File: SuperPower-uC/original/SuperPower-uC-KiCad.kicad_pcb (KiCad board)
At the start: 2 copper layers, 95 x 42 mm, 172 parts, among them J1 JST_PH_S2B_thru, J11 Conn_01x02_Male, J12 Conn_01x02_Male, J13 Conn_01x02_Male, J2 Barrel_Jack_Switch, J3 Conn_01x02_Male, J4 DNP/JST_ZH_S2B_thru, J5 JST_XH_S2B_thru, J6 Conn_01x02_Male, J7 Conn_01x19_Female, J8 Conn_01x19_Female, Q1 DMN2019UTS, Q10 2N7002A, Q11 2N7002A, Q12 DMP2035UVT, Q13 DMP2035UVT, Q14 DMP2035UVT, Q2 DMP3028LSD, Q3 DMN3018SSD, Q4 2N7002A, Q5 DMP2035UVT, Q6 BSS84-7-F, Q7 S8050, Q8 S8050, Q9 2N7002A, SW1 DNP/SKRKAEE020, U1 AP9101CK6-AYTRG1, U10 TPS63070RNMT, U2 USB-C, U3 IP4220CZ6, U4 LTC4162EUFD-LAD, U5 RV-3028-C7, U6 CP2102N-A01-GQFN28, U7 ESP32-WROOM32, U8 TPS70933DRVT, U9 TPS63070RNMT

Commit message: Update Placement + Add some labels
+3.3V Buck-Boost DC-DC converter
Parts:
- moved TP17 57.2 mm to (165.8, 64.5)
- moved TP5 26.2 mm to (120.8, 62.8)
- moved JP2 17.8 mm to (182.2, 60.2)
- moved R25 11.6 mm to (171.8, 64.2), turned to 0 degrees
- moved TP4 11.3 mm to (108.2, 56.0)
- moved TP7 8.88 mm to (102.0, 46.2)
- moved C24 8.67 mm to (172.8, 50.8), turned to 270 degrees
- moved TP6 8.30 mm to (102.0, 49.2)
- moved R54 7.24 mm to (179.5, 63.5), turned to 0 degrees
- moved R50 6.46 mm to (175.5, 50.0), turned to 180 degrees
- moved C19 6.15 mm to (172.8, 55.2), turned to 90 degrees
- moved Q10 5.54 mm to (175.8, 63.2), turned to 90 degrees
- moved R46 3.69 mm to (179.5, 53.2), turned to 0 degrees
- moved R42 3.62 mm to (179.0, 59.2), turned to 90 degrees
- moved C26 3.06 mm to (172.8, 46.8)
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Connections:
- net Net-(C16-Pad1) renamed /Regulator and Cut-Off Module/3v3_Vin
- net Net-(C22-Pad1) renamed /Regulator and Cut-Off Module/3v3_Vaux
- net Net-(JP2-Pad1) renamed /Regulator and Cut-Off Module/3v3_OnOff
- net Net-(L2-Pad1) renamed /Regulator and Cut-Off Module/3v3_L2
- net Net-(L2-Pad2) renamed /Regulator and Cut-Off Module/3v3_L1
- net Net-(Q5-Pad3) renamed /Regulator and Cut-Off Module/3v3_OnOff_Gate
- net Net-(R44-Pad1) renamed /Regulator and Cut-Off Module/3v3_EN
- net Net-(R46-Pad1) renamed /Regulator and Cut-Off Module/3v3_PG
- net Net-(R47-Pad2) renamed /Regulator and Cut-Off Module/3v3_FB

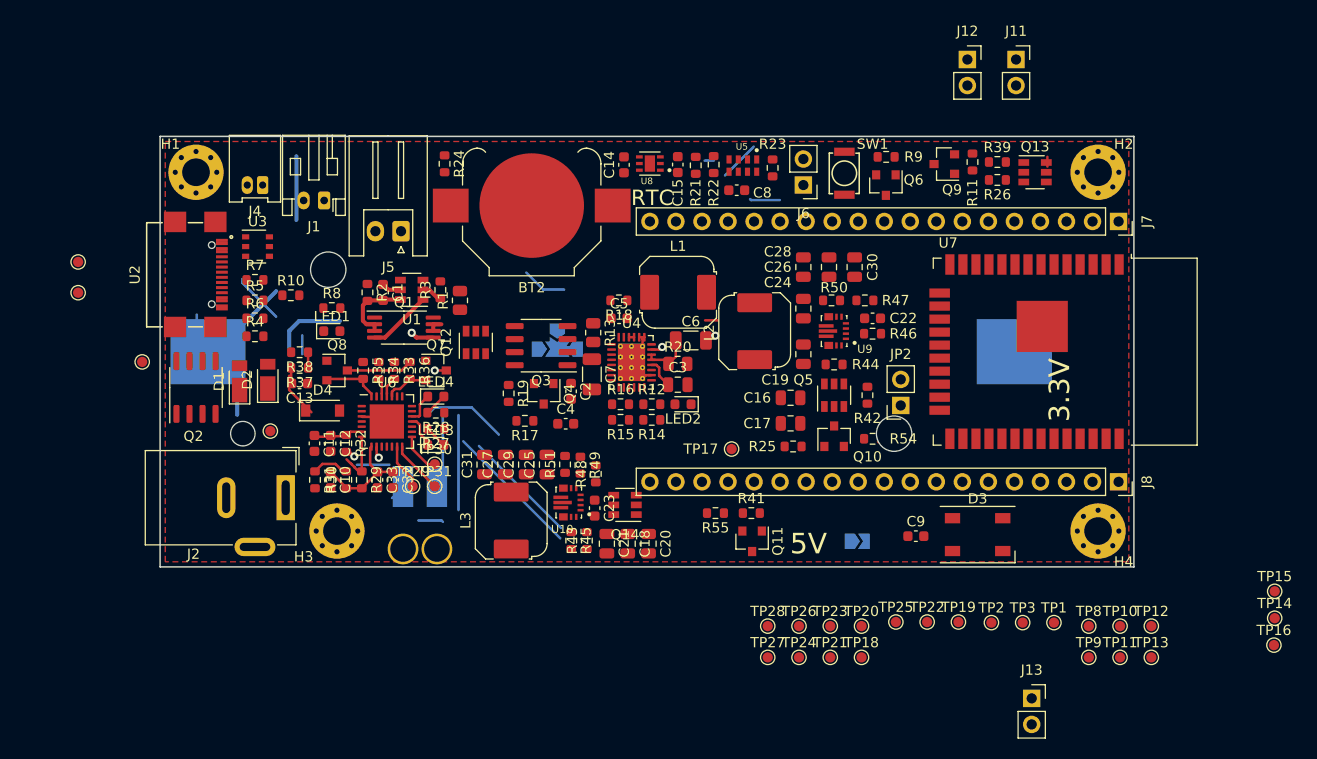
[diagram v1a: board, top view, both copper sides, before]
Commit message: Update Placement USB_UART_Bridge
+ Misc.
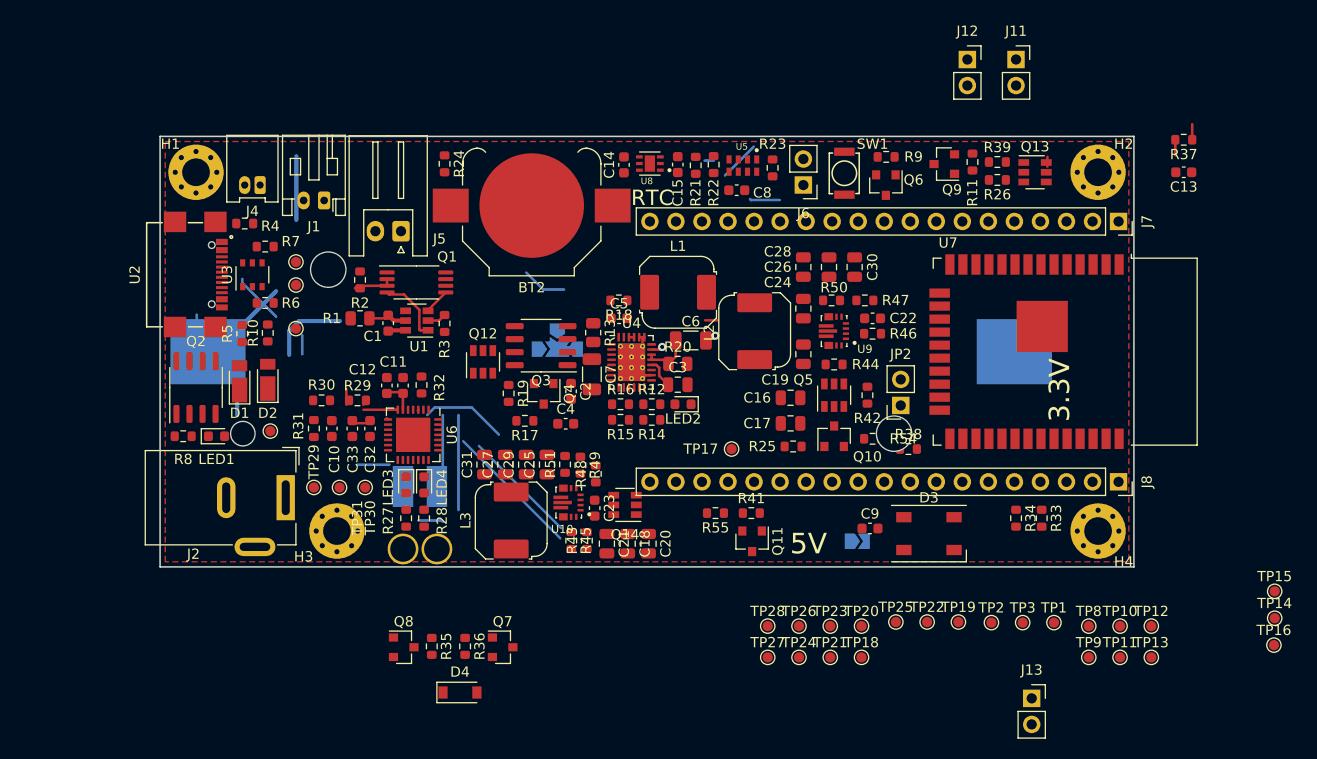
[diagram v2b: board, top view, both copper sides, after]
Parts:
- moved R37 89.1 mm to (209.9, 34.3)
- moved C13 88.7 mm to (209.9, 37.5)
- moved R33 64.8 mm to (196.0, 71.2)
- moved R34 63.8 mm to (193.5, 71.2)
- moved R38 60.1 mm to (183.0, 64.5), turned to 0 degrees
- moved D4 30.6 mm to (139.2, 88.2)
- moved Q7 27.8 mm to (143.4, 83.8)
- moved Q8 27.8 mm to (133.8, 83.8)
- moved R35 27.7 mm to (136.5, 83.8)
- moved R36 27.4 mm to (139.8, 83.8)
- moved TP6 21.3 mm to (123.2, 48.5)
- moved TP7 21.2 mm to (123.2, 46.2)
- moved R8 19.1 mm to (112.2, 63.2), turned to 180 degrees
- moved TP4 15.3 mm to (123.2, 52.8)
- moved LED1 15.2 mm to (115.5, 63.2)
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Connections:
- net Net-(C10-Pad1) renamed /MCU Module/Vbus
- net Net-(Q1-Pad4) renamed /Battery Module/DO
- net Net-(Q1-Pad5) renamed /Battery Module/CO
- net Net-(R3-Pad1) renamed /Battery Module/VM
- net Net-(R4-Pad1) renamed /Charger inputs and USB IO/Shield
- net Net-(R6-Pad1) renamed /Charger inputs and USB IO/CC2
- net Net-(R7-Pad1) renamed /Charger inputs and USB IO/CC1
- net Net-(TP29-Pad1) renamed /MCU Module/CHREN
- net Net-(TP30-Pad1) renamed /MCU Module/CHR0
- net Net-(TP31-Pad1) renamed /MCU Module/CHR1
- R37 pad 1: /MCU Module/3v3_MCU -> /MCU Module/EN
- R37 pad 2: /MCU Module/EN -> /MCU Module/3v3_MCU
- R38 pad 1: /MCU Module/3v3_MCU -> /MCU Module/IO0
- R38 pad 2: /MCU Module/IO0 -> /MCU Module/3v3_MCU
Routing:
- net /MCU Module/Vbus: track 10.4 -> 3.31 mm
- net Net-(Q8-Pad3): track 6.45 -> 0.00 mm
- net Net-(Q1-Pad5): track 0.00 -> 6.22 mm
- net /Battery Module/CO: track 8.52 -> 2.51 mm, vias 1 -> 0
- net /MCU Module/DTR: track 5.38 -> 0.00 mm
- net /MCU Module/CHR1: track 5.19 -> 0.00 mm
- net /MCU Module/CHREN: track 4.50 -> 0.00 mm
- net /MCU Module/EN: track 6.00 -> 1.52 mm
- net /MCU Module/RTS: track 4.32 -> 0.00 mm
- net /MCU Module/CHR0: track 4.00 -> 0.00 mm
- net Net-(R30-Pad2): track 3.65 -> 0.00 mm
- net GND: track 11.8 -> 8.44 mm
- net /MCU Module/RXT: track 3.19 -> 0.00 mm
- net /MCU Module/TXT: track 2.98 -> 0.00 mm
- net Net-(LED4-Pad2): track 2.26 -> 0.00 mm
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
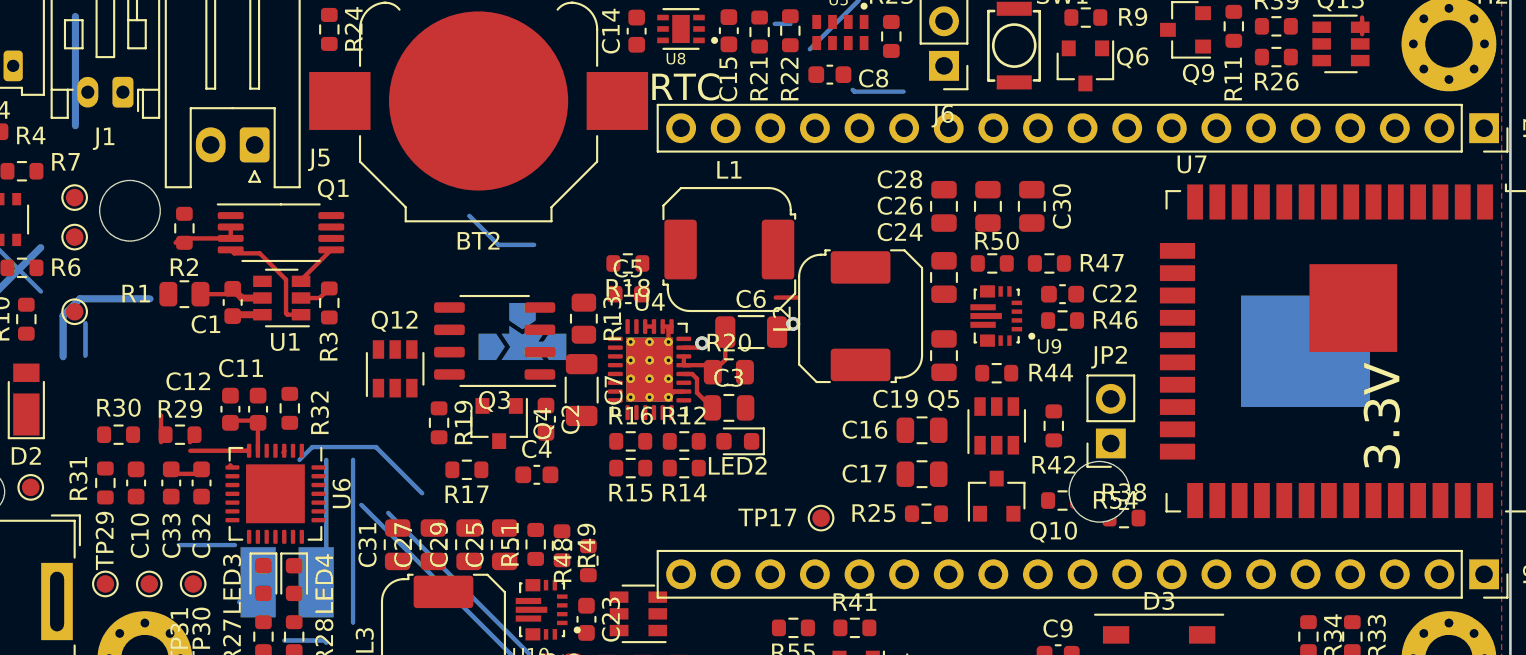
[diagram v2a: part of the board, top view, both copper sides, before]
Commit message: Update LTC4162-L components placement
+ Misc.
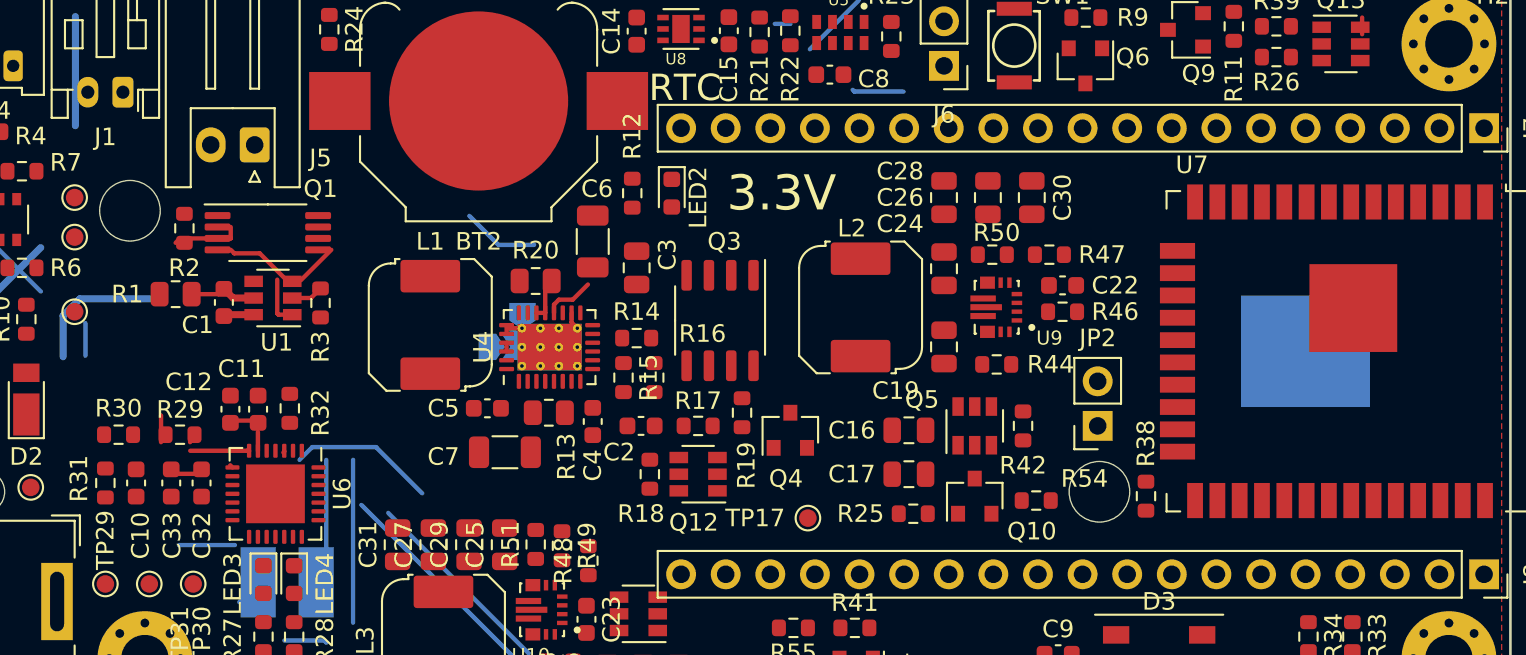
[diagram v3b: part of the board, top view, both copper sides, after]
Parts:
- moved Q12 18.3 mm to (158.8, 62.0), turned to 180 degrees
- moved L1 17.6 mm to (143.5, 53.5), turned to 90 degrees
- moved R19 17.3 mm to (161.2, 58.5), turned to 90 degrees
- moved Q4 16.6 mm to (164.0, 59.5), turned to 90 degrees
- moved LED2 14.6 mm to (157.2, 46.0), turned to 270 degrees
- moved R12 14.4 mm to (155.0, 46.0), turned to 90 degrees
- moved R17 13.4 mm to (158.8, 59.2), turned to 0 degrees
- moved Q3 12.9 mm to (160.0, 53.2), turned to 270 degrees
- moved R20 12.2 mm to (149.5, 51.0), turned to 180 degrees
- moved R18 12.1 mm to (156.0, 62.0), turned to 90 degrees
- moved C6 10.4 mm to (152.8, 48.8), turned to 90 degrees
- moved C5 10.3 mm to (146.8, 58.2), turned to 180 degrees
- moved C3 9.55 mm to (155.2, 50.2), turned to 90 degrees
- moved R14 7.88 mm to (155.2, 54.2)
- moved U4 5.83 mm to (150.3, 54.8), turned to 90 degrees
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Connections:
- net Net-(C5-Pad1) renamed /Charging Module/BOOST
- net Net-(C5-Pad2) renamed /Charging Module/SW
- net Net-(L1-Pad2) renamed /Charging Module/CSP
- net Net-(LED2-Pad1) renamed /Charging Module/~SMBALERT_LED
- net Net-(Q12-Pad3) renamed /Charging Module/Vgate
- net Net-(Q3-Pad2) renamed /Charging Module/IN_FET
- net Net-(Q3-Pad4) renamed /Charging Module/BAT_FET
- net Net-(Q3-Pad7) renamed /Charging Module/CLP
- net Net-(R14-Pad2) renamed /Charging Module/RT
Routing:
- net /Charging Module/CSP: track 6.76 -> 0.00 mm, vias 2 -> 0
- net Net-(L1-Pad2): track 0.00 -> 4.37 mm
- net /Battery Module/DO: track 6.66 -> 2.81 mm
- net /Battery Module/CO: track 2.51 -> 6.36 mm
- net +BATT: track 24.4 -> 21.8 mm

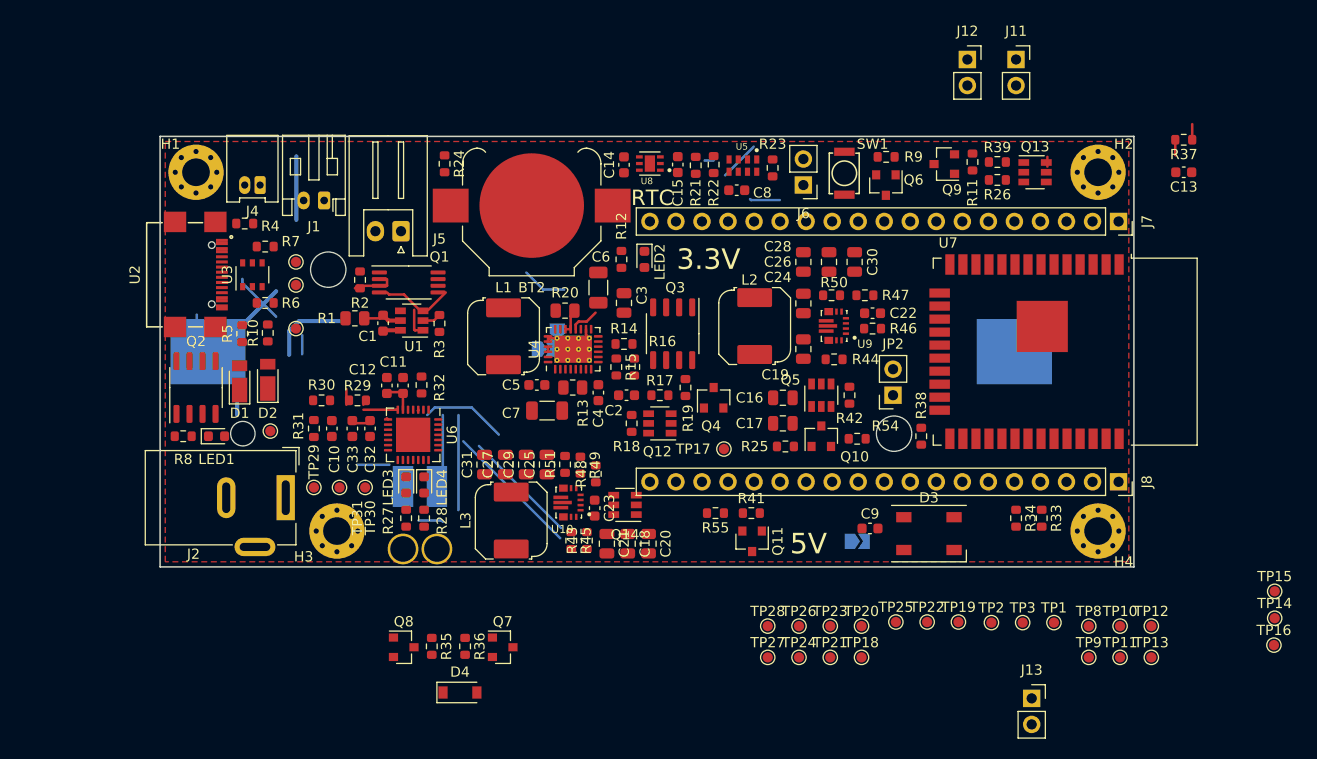
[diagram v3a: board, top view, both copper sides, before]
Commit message: Update components Placement
+5V Buck-Boost + Misc.
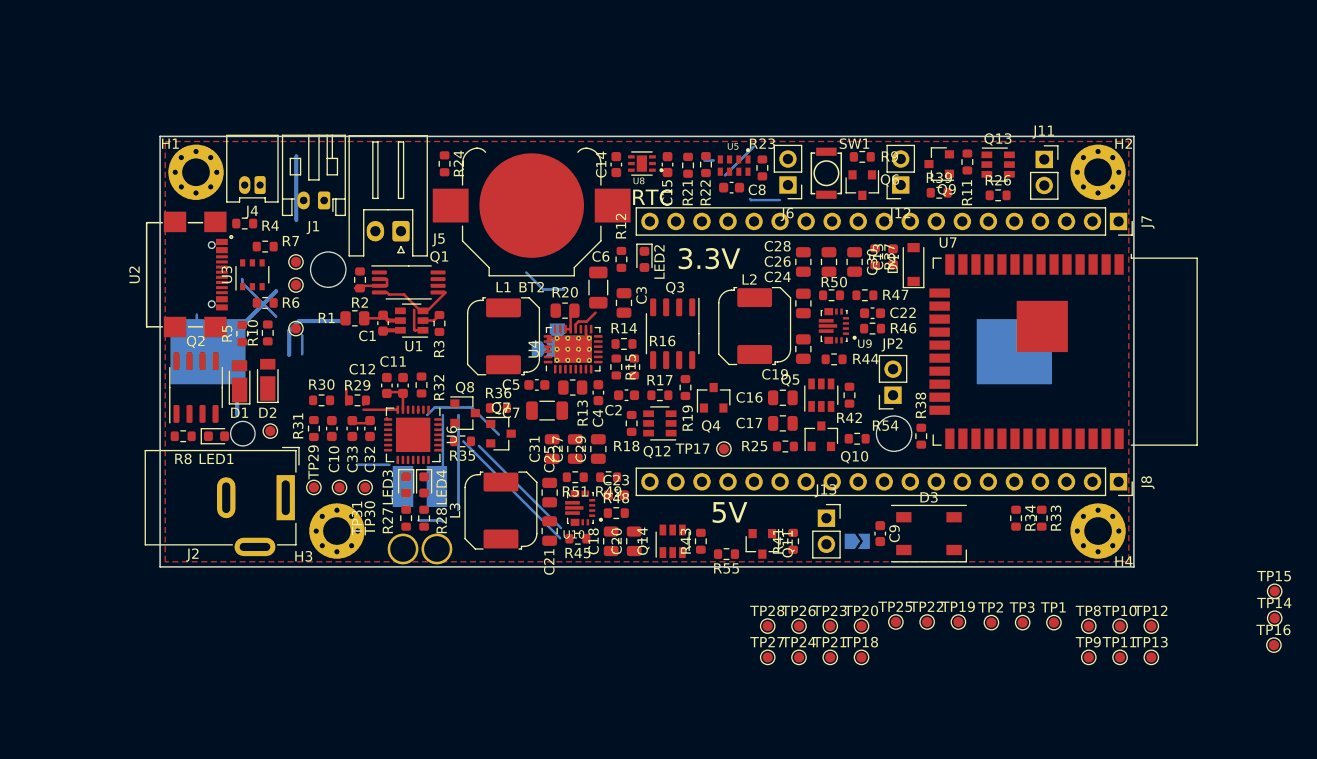
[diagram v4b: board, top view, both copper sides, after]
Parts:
- moved D4 60.8 mm to (183.5, 46.5), turned to 90 degrees
- moved R37 32.2 mm to (179.8, 45.8), turned to 270 degrees
- moved C13 29.5 mm to (181.5, 45.8), turned to 90 degrees
- moved J13 26.6 mm to (175.0, 71.2)
- moved Q8 23.6 mm to (139.8, 61.0)
- moved R36 23.5 mm to (143.0, 60.5), turned to 0 degrees
- moved Q7 20.8 mm to (143.2, 63.0)
- moved R35 20.2 mm to (139.5, 63.8), turned to 180 degrees
- moved J12 13.9 mm to (182.2, 38.8), turned to 180 degrees
- moved R43 11.1 mm to (162.8, 73.5)
- moved J11 10.1 mm to (196.2, 36.2)
- moved C29 7.20 mm to (152.8, 64.5)
- moved C27 6.99 mm to (150.5, 64.5)
- moved C31 6.78 mm to (148.2, 64.5)
- moved R39 6.42 mm to (186.0, 39.5)
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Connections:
- net Net-(C18-Pad1) renamed /Regulator and Cut-Off Module/5V_Vin
- net Net-(C23-Pad1) renamed /Regulator and Cut-Off Module/5V_Vaux
- net Net-(L3-Pad1) renamed /Regulator and Cut-Off Module/5V_L2
- net Net-(L3-Pad2) renamed /Regulator and Cut-Off Module/5V_L1
- net Net-(R45-Pad1) renamed /Regulator and Cut-Off Module/5V_EN
- net Net-(R48-Pad1) renamed /Regulator and Cut-Off Module/5V_PG
- net Net-(R49-Pad2) renamed /Regulator and Cut-Off Module/5V_FB
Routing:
- net /MCU Module/3v3_MCU: track 1.54 -> 0.00 mm
- net /MCU Module/EN: track 1.52 -> 0.00 mm
- net /MCU Module/3v3: track 0.95 -> 0.00 mm
